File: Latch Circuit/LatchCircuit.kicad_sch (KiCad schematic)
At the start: 24 parts

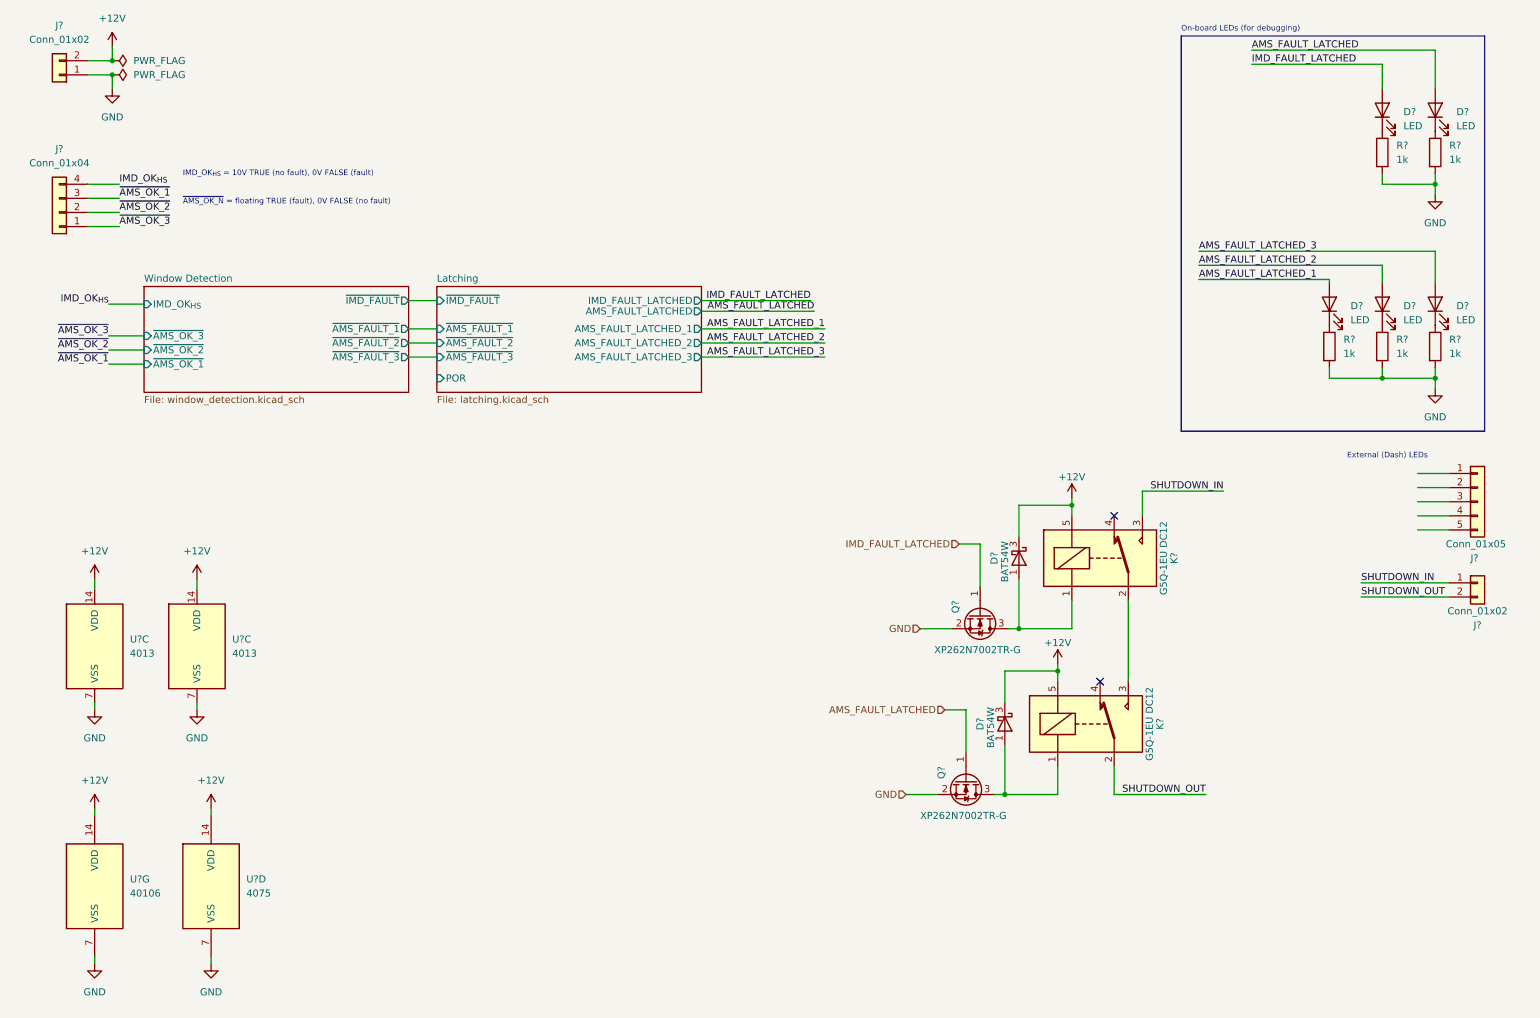
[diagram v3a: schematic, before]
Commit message: update schematic (ESF v1 submission)
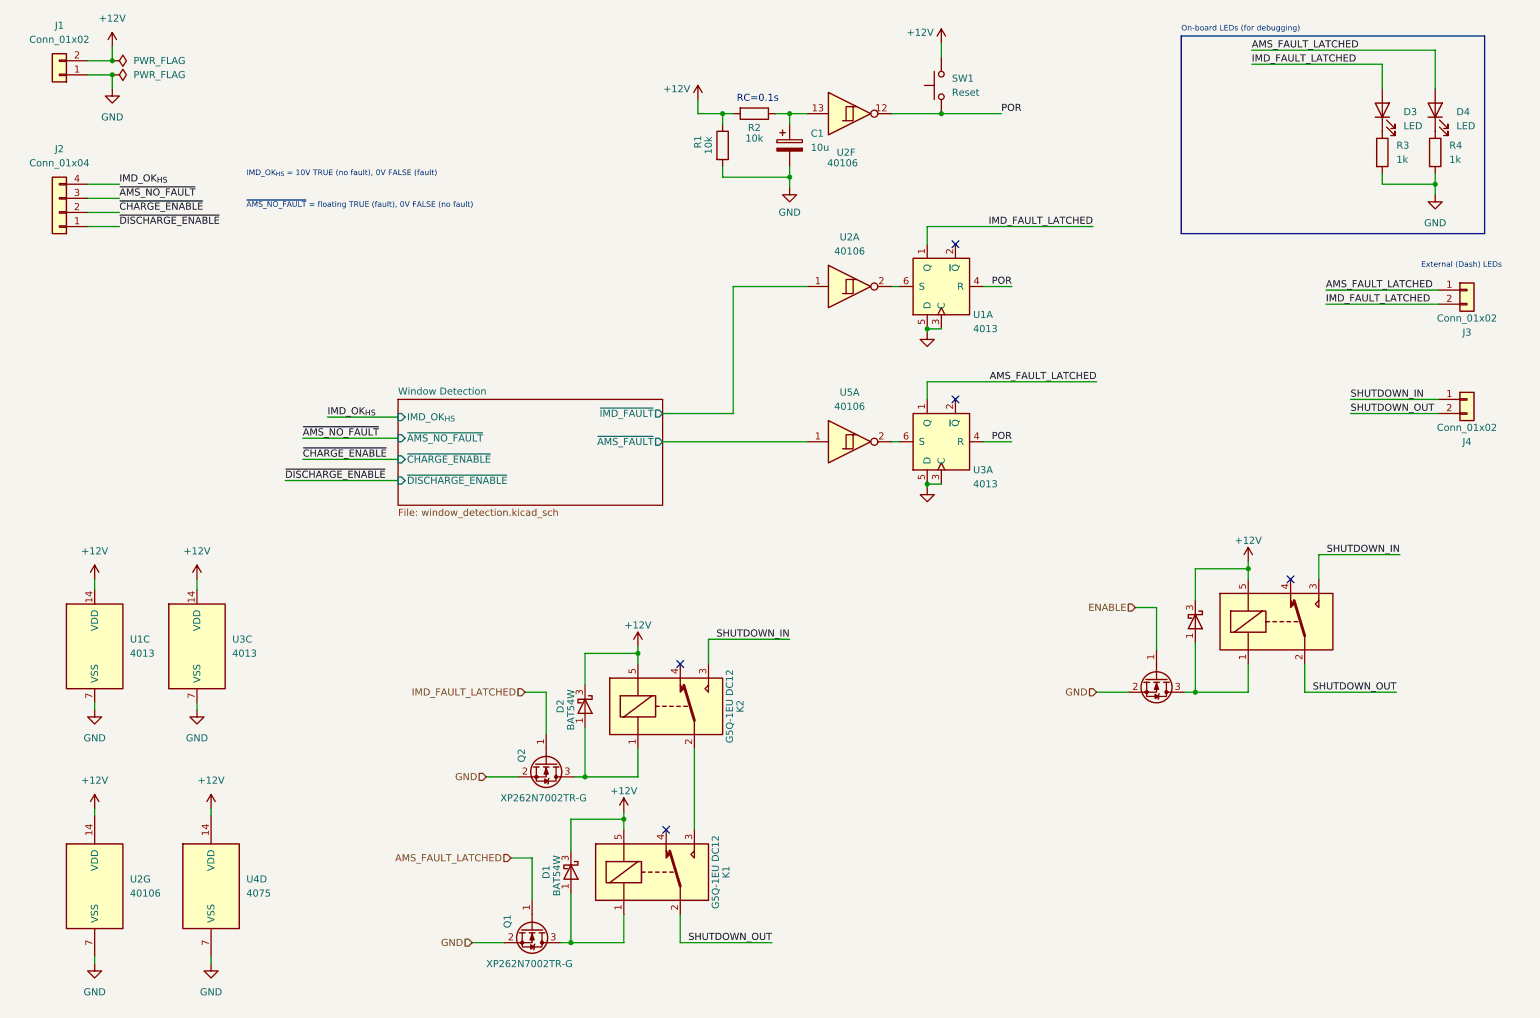
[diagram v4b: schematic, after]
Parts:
- removed D? (x3): LED, LED_THT:LED_D5.0mm, symbol Device:LED
- removed J?: Conn_01x04, symbol Connector_Generic:Conn_01x04
- removed J?: Conn_01x05, symbol Connector_Generic:Conn_01x05
- removed R? (x3): 1k, Resistor_THT:R_Axial_DIN0309_L9.0mm_D3.2mm_P15.24mm_Horizontal, symbol Device:R
- added C1: 10u, Capacitor_THT:CP_Radial_D5.0mm_P2.00mm, symbol Device:C_Polarized
- added D?: BAT54W, Package_TO_SOT_SMD:SOT-323_SC-70, symbol Diode:BAT54W
- added J2: Conn_01x04, symbol Connector_Generic:Conn_01x04
- added J3: Conn_01x02, Connector_Molex:Molex_Micro-Fit_3.0_43650-0200_1x02_P3.00mm_Horizontal, symbol Connector_Generic:Conn_01x02
- added K?: G5Q-1EU DC12, Relay_THT:Relay_SPDT_Omron-G5Q-1, symbol Relay:G5Q-1
- added Q?: XP262N7002TR-G, Package_TO_SOT_SMD:SOT-23, symbol Device:Q_NMOS_GSD
- added R1, R2: 10k, Resistor_SMD:R_0603_1608Metric, symbol Device:R
- added SW1: Reset, symbol Switch:SW_Push
- added unit 1 of U1
- added unit 6 of U2
- added unit 1 of U2
- added unit 1 of U3
- added U5: 40106, symbol 4xxx:40106
- gave numbers to parts that had none: 16
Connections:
- net +12V: now also D?.3 (K), K?.5, R1.1, R2.2, SW1.2
- net AMS_FAULT_LATCHED: now also J3.1 (Pin_1), U3.1 (Q)
- net GND: now also C1.2, Q?.2 (S), R1.2, U1.3 (C), U1.5 (D), U3.3 (C), U3.5 (D)
- net IMD_FAULT_LATCHED: now also J3.2 (Pin_2), U1.1 (Q)
- net IMD_OK_{HS}: now also J2.4 (Pin_4)
- net SHUTDOWN_IN: now also K?.3
- net SHUTDOWN_OUT: now also K?.2
- new net: D?.1 (A), K?.1, Q?.3 (D)
- new net: U3.6 (S), U5.2
- new net: C1.1, R2.1, U2.13
- new net: U1.6 (S), U2.2
- new net ENABLE: Q?.1 (G)
- new net POR: SW1.1, U1.4 (R), U2.12, U3.4 (R)
- new net Window Detection/~{AMS_FAULT}: U5.1
- new net Window Detection/~{IMD_FAULT}: U2.1
- new net ~{AMS_NO_FAULT}: J2.3 (Pin_3)
- new net ~{CHARGE_ENABLE}: J2.2 (Pin_2)
- new net ~{DISCHARGE_ENABLE}: J2.1 (Pin_1)
- no-connect marks 2 -> 5
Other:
- removed sheet Latching
- sheet Window Detection ports: added ~{AMS_FAULT}, ~{AMS_NO_FAULT}, ~{CHARGE_ENABLE}, ~{DISCHARGE_ENABLE}; removed ~{AMS_FAULT_1}, ~{AMS_FAULT_2}, ~{AMS_FAULT_3}, ~{AMS_OK_1}, ~{AMS_OK_2}, ~{AMS_OK_3}
- note added: "RC=0.1s"
- note added: "~{AMS_NO_FAULT} = floating TRUE (fault), 0V FALSE (no fault)"
- note removed: "~{AMS_OK_N} = floating TRUE (fault), 0V FALSE (no fault)"
- moved on the sheet: D1, D2, J4, K1, K2, Q1, Q2

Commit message: update schematic
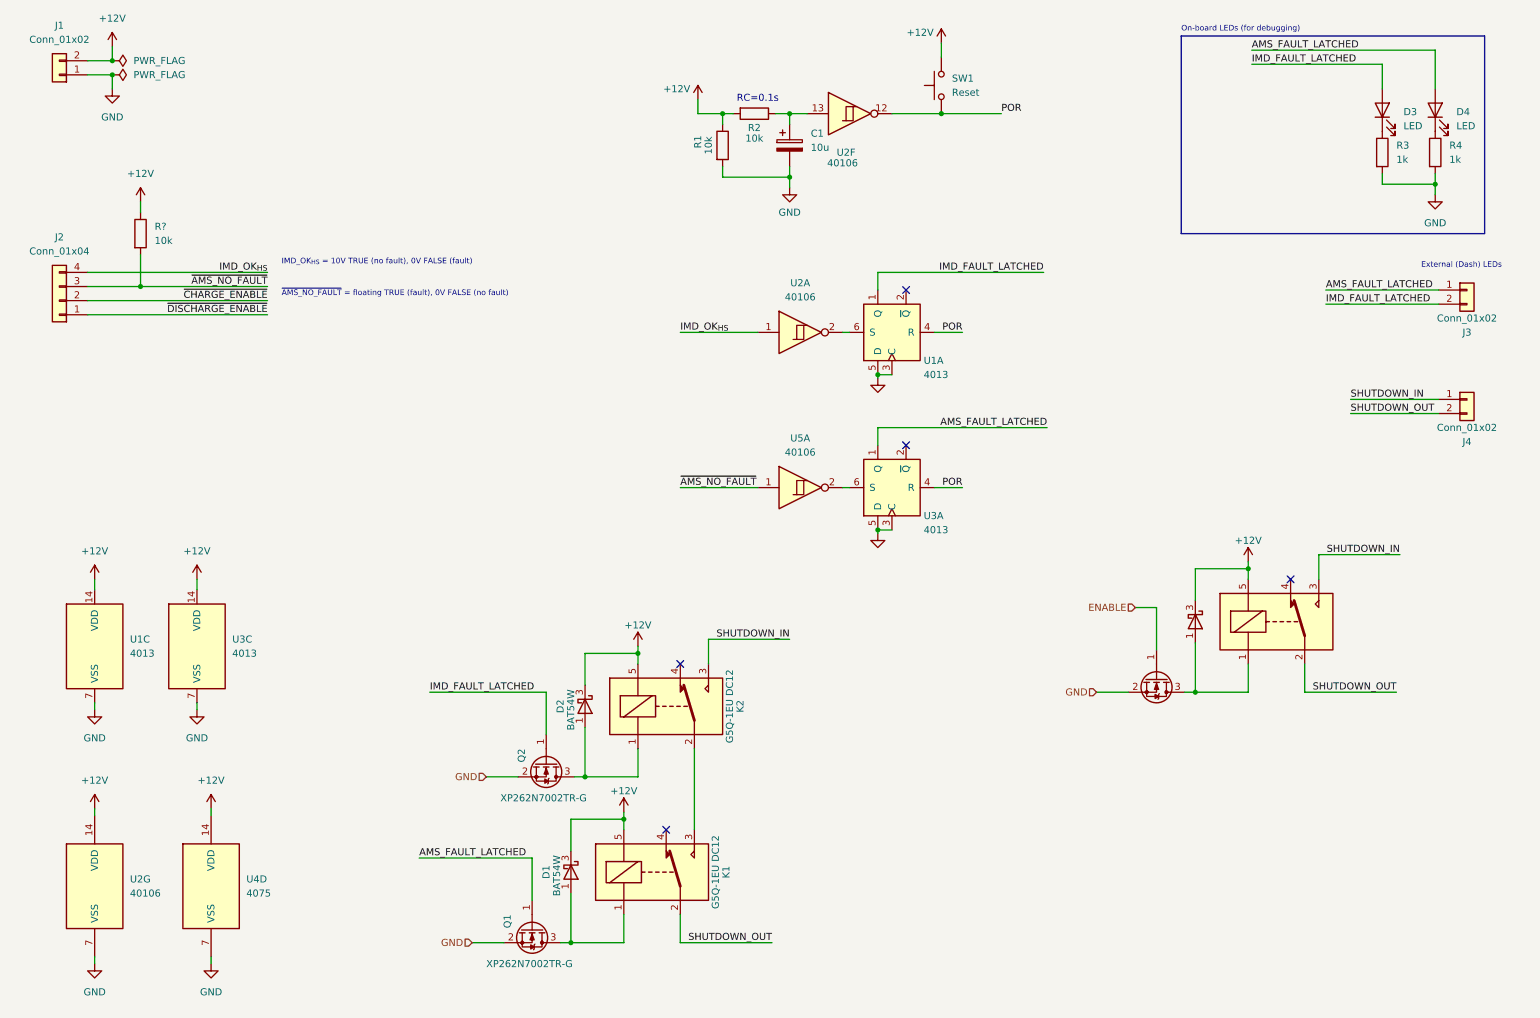
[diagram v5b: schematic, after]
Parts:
- added R?: 10k, Resistor_THT:R_Axial_DIN0309_L9.0mm_D3.2mm_P15.24mm_Horizontal, symbol Device:R
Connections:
- net Window Detection/~{AMS_FAULT} is gone; now on net ~{AMS_NO_FAULT}: U5.1
- net Window Detection/~{IMD_FAULT} is gone; now on net IMD_OK_{HS}: U2.1
- net +12V: now also R?.1
- net ~{AMS_NO_FAULT}: now also R?.2
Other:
- removed sheet Window Detection
- moved on the sheet: J2, U1A, U2A, U3A, U5A

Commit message: remove superfluous relay
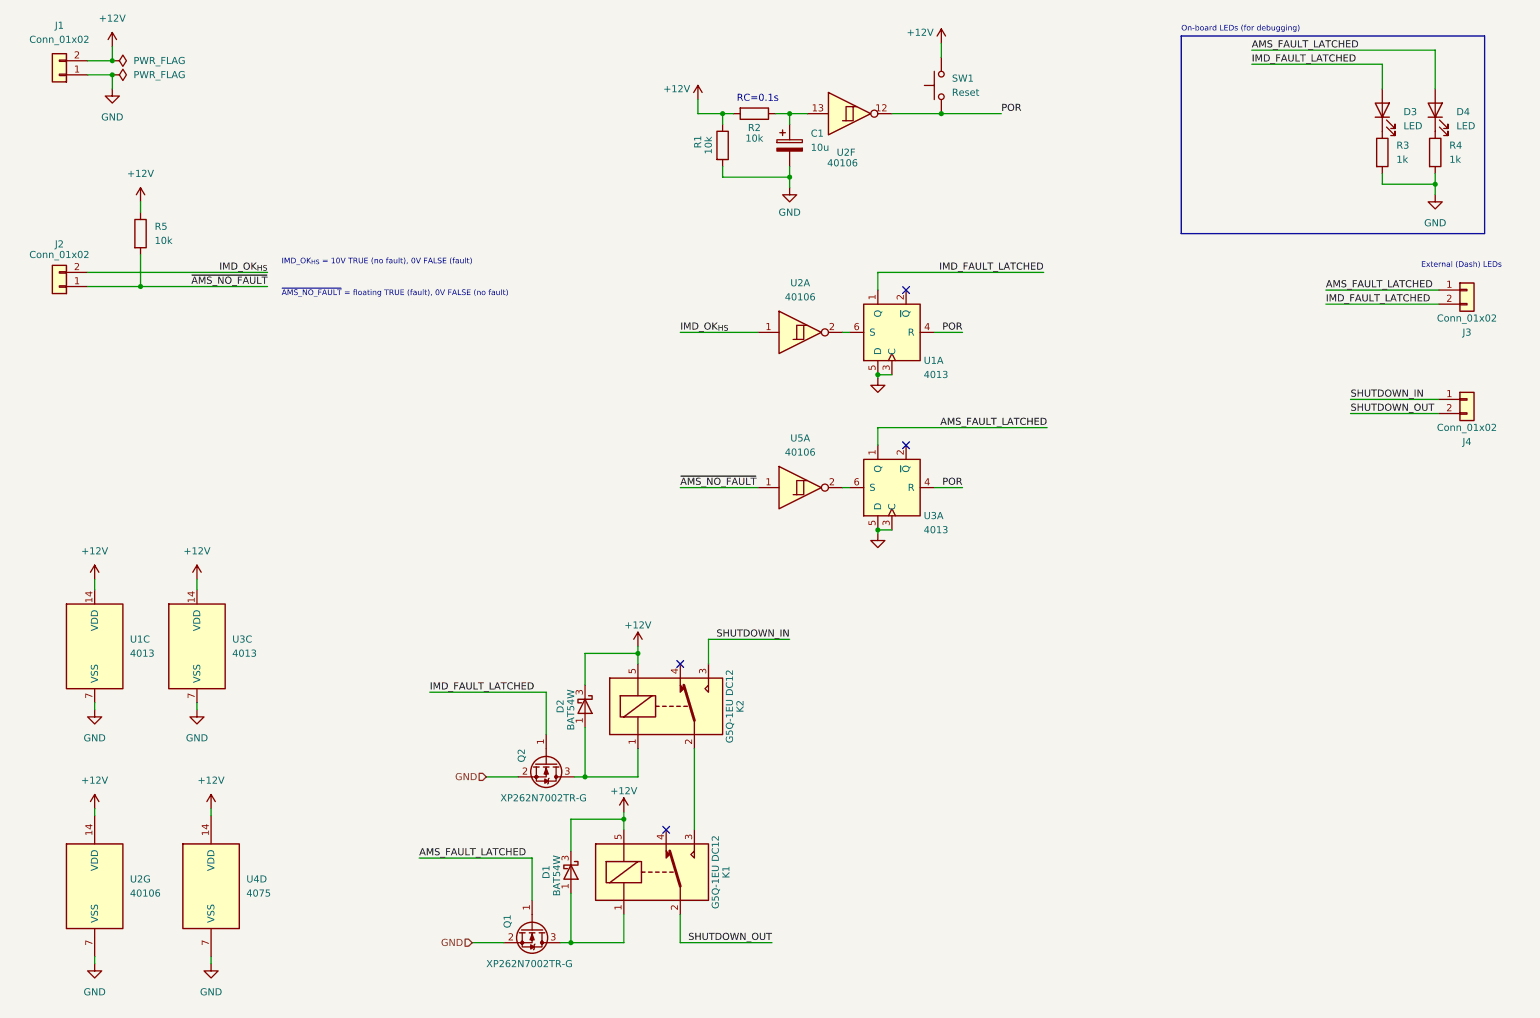
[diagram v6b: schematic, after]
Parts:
- removed D?: BAT54W, Package_TO_SOT_SMD:SOT-323_SC-70, symbol Diode:BAT54W
- removed J2: Conn_01x04, symbol Connector_Generic:Conn_01x04
- removed K?: G5Q-1EU DC12, Relay_THT:Relay_SPDT_Omron-G5Q-1, symbol Relay:G5Q-1
- removed Q?: XP262N7002TR-G, Package_TO_SOT_SMD:SOT-23, symbol Device:Q_NMOS_GSD
- added J2: Conn_01x02, Connector_Molex:Molex_Micro-Fit_3.0_43650-0200_1x02_P3.00mm_Horizontal, symbol Connector_Generic:Conn_01x02
- gave numbers to parts that had none: 1
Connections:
- net IMD_OK_{HS}: now also J2.2 (Pin_2)
- net ~{AMS_NO_FAULT}: now also J2.1 (Pin_1)
- no-connect marks 5 -> 4

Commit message: update schematic; add WIP pcb
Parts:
- removed unit 3 of U3
- removed U4: 4075, symbol 4xxx:4075
- added C1, C2: 100n, Capacitor_SMD:C_0603_1608Metric_Pad1.08x0.95mm_HandSolder, symbol Device:C_Small
- added D3: LED, LED_SMD:LED_0805_2012Metric_Pad1.15x1.40mm_HandSolder, symbol Device:LED
- added H1, H2, H3, H4: MountingHole, MountingHole:MountingHole_2.2mm_M2, symbol Mechanical:MountingHole
- added R4: 1k, Resistor_SMD:R_0603_1608Metric_Pad0.98x0.95mm_HandSolder, symbol Device:R
- added unit 2 of U2
- D4: renamed from D3; footprint LED_THT:LED_D5.0mm -> LED_SMD:LED_0805_2012Metric_Pad1.15x1.40mm_HandSolder
- D5: renamed from D4; footprint LED_THT:LED_D5.0mm -> LED_SMD:LED_0805_2012Metric_Pad1.15x1.40mm_HandSolder
- J1: value Conn_01x02 -> 12V_Power
- J2: value Conn_01x02 -> IMD_AMS
- J3: value Conn_01x02 -> ExternalLEDs
- J4: value Conn_01x02 -> Shutdown
- R1: renamed from R5; footprint Resistor_THT:R_Axial_DIN0309_L9.0mm_D3.2mm_P15.24mm_Horizontal -> Resistor_SMD:R_0603_1608Metric_Pad0.98x0.95mm_HandSolder
- R2: renamed from R1; footprint Resistor_SMD:R_0603_1608Metric -> Resistor_SMD:R_0603_1608Metric_Pad0.98x0.95mm_HandSolder
- R3: renamed from R2; footprint Resistor_SMD:R_0603_1608Metric -> Resistor_SMD:R_0603_1608Metric_Pad0.98x0.95mm_HandSolder
- R5: renamed from R3; footprint Resistor_THT:R_Axial_DIN0309_L9.0mm_D3.2mm_P15.24mm_Horizontal -> Resistor_SMD:R_0603_1608Metric_Pad0.98x0.95mm_HandSolder
- R6: renamed from R4; footprint Resistor_THT:R_Axial_DIN0309_L9.0mm_D3.2mm_P15.24mm_Horizontal -> Resistor_SMD:R_0603_1608Metric_Pad0.98x0.95mm_HandSolder
- SW1: footprint (none) -> Connector_Molex:Molex_Micro-Fit_3.0_43650-0200_1x02_P3.00mm_Horizontal
- U1: renamed from U3; footprint (none) -> Package_SO:SOIC-14_3.9x8.7mm_P1.27mm
- U1, U2: footprint (none) -> Package_SO:SOIC-14_3.9x8.7mm_P1.27mm
- U2: renamed from U5; footprint (none) -> Package_SO:SOIC-14_3.9x8.7mm_P1.27mm
- renumbered C1 to C4
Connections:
- net +12V: now also C1.1, C2.1, D3.2 (A)
- net GND: now also U1.11 (C), U1.9 (D), C1.2, C2.2, R4.2; no longer U1.3 (C), U1.5 (D)
- net POR: now also U1.10 (R), U2.8; no longer U1.4 (R), U2.12
- net ~{AMS_NO_FAULT}: now also U2.5; no longer U2.1
- net at C4.1, R3.1: now also U2.9; no longer U2.13
- net at U2.2: now also U2.3; no longer U1.6 (S)
- net AMS_FAULT_LATCHED renamed AMS_OK_LATCHED
- net AMS_OK_LATCHED: now also U1.13 (Q); no longer U1.1 (Q)
- net IMD_FAULT_LATCHED renamed IMD_OK_LATCHED
- new net: D3.1 (K), R4.1
- new net: U1.8 (S), U2.6
- new net: U1.6 (S), U2.4
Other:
- note added: "IC Power"
- note added: "Mounting Holes"
- note added: "Outputs To External Connections"
- moved on the sheet: J3, J4, U1C, U2G
